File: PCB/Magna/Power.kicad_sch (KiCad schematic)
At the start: 32 parts, among them U902 XL1509-ADJ, U903 WS3222D, U905 AP2171W

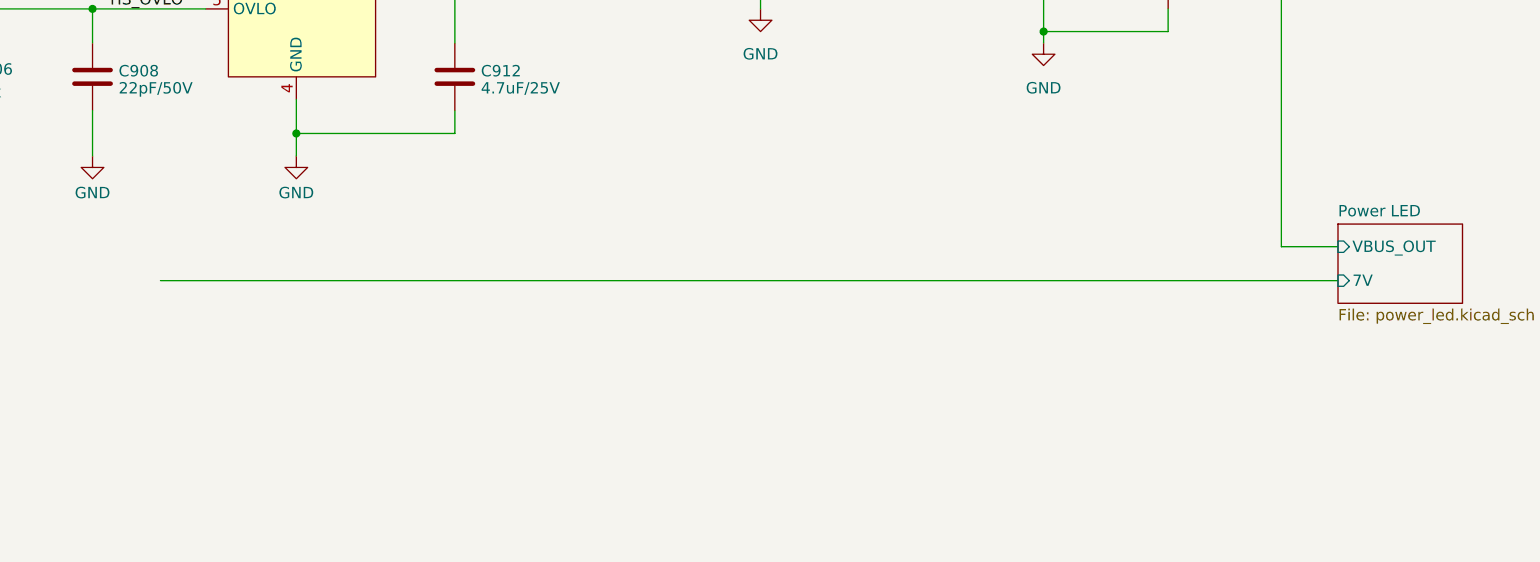
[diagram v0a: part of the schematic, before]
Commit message: Update Audio connector pinning (#14)
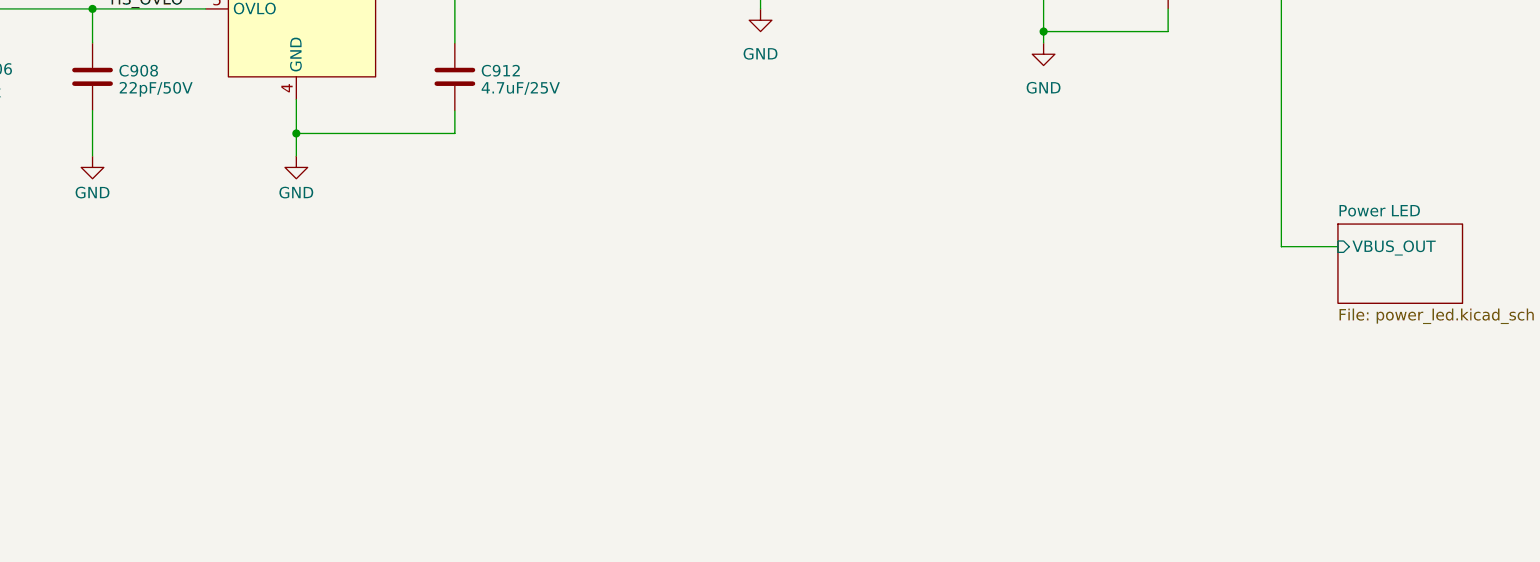
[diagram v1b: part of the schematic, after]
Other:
- sheet Power LED ports: added none; removed 7V
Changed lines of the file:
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@@
-    (stroke (width 0) (type default))
-  )
-  (wire (pts (xy 132.08 80.01) (xy 264.16 80.01))
     (stroke (width 0) (type default))
   )
@@
       (effects (font (size 1.27 1.27)) (justify left top))
     )
-    (pin "7V" input (at 264.16 80.01 180)
-      (effects (font (size 1.27 1.27)) (justify left))
-    )
     (pin "VBUS_OUT" input (at 264.16 76.2 180)

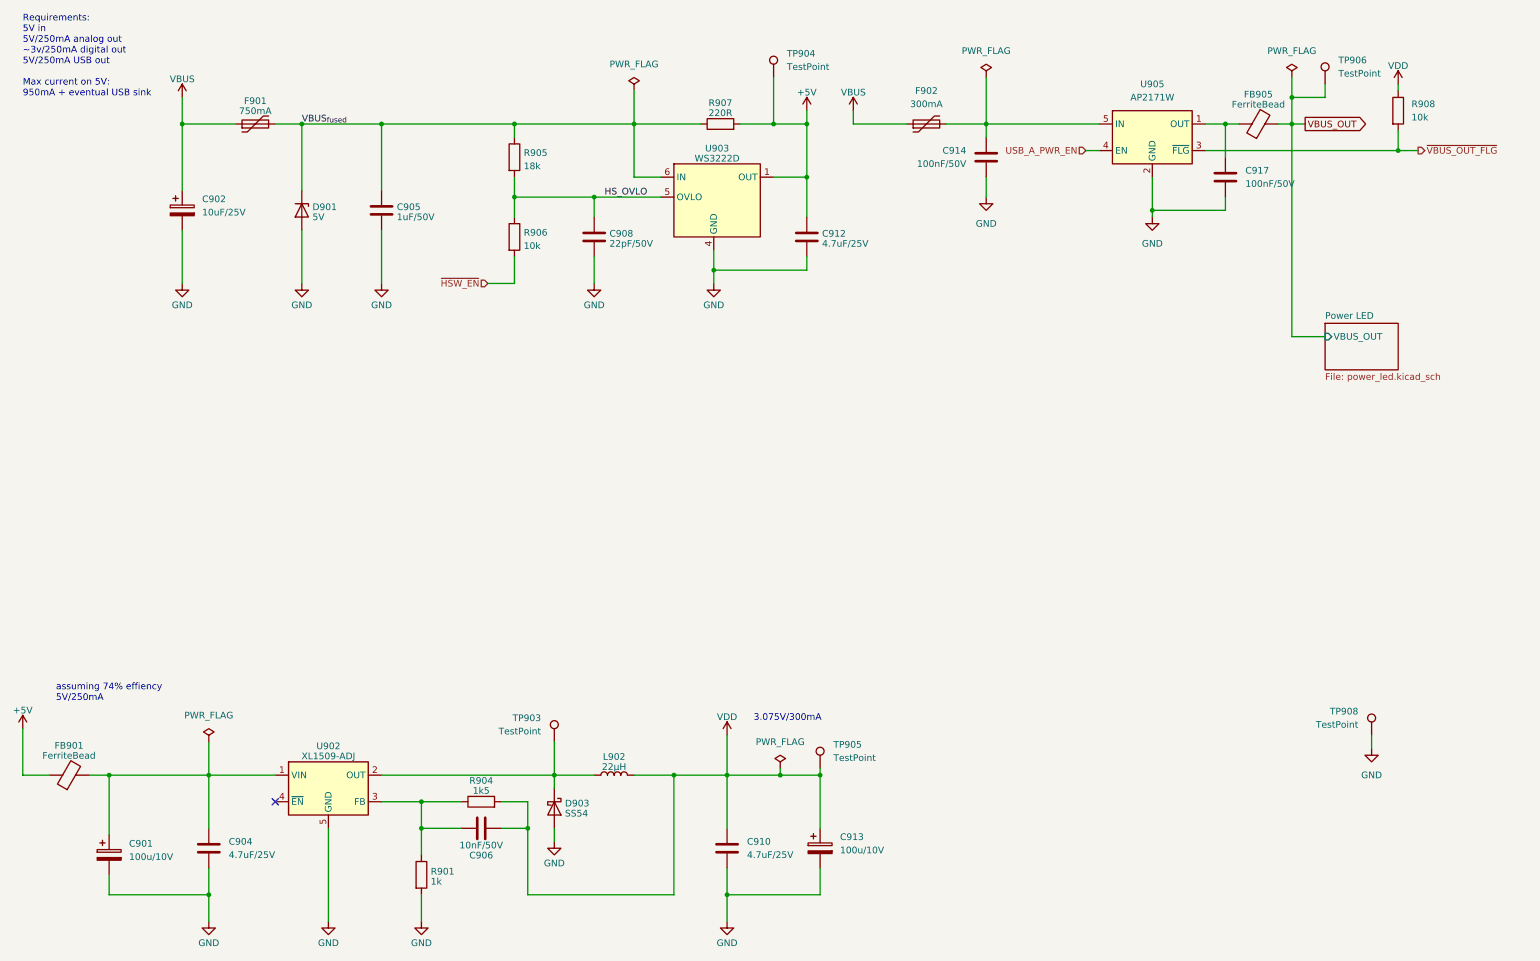
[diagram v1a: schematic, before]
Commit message: Change components on Main Board to use more of the same part#
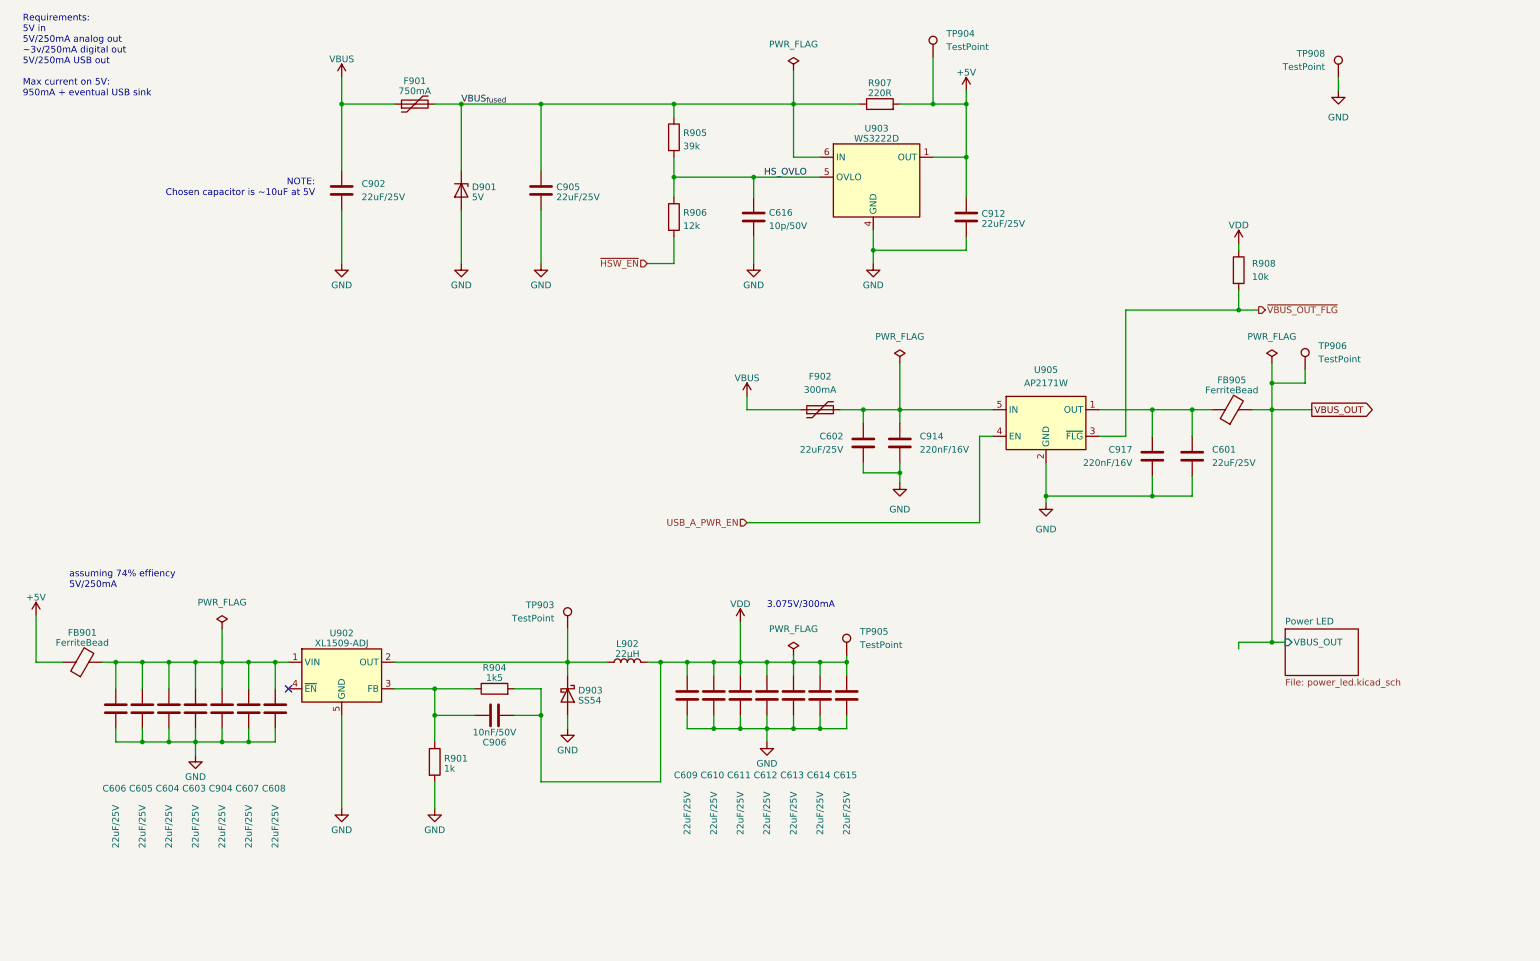
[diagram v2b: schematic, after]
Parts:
- removed C901, C913: 100u/10V, Capacitor_SMD:CP_Elec_6.3x5.8, symbol Device:C_Polarized
- removed C908: 22pF/50V, Capacitor_SMD:C_0805_2012Metric_Pad1.18x1.45mm_HandSolder, symbol Device:C
- removed C910: 4.7uF/25V, Capacitor_SMD:C_0805_2012Metric_Pad1.18x1.45mm_HandSolder, symbol Device:C
- added C601, C602, C603, C604, C605, C606, C607, C608, C609, C610, C611, C612, C613, C614, C615: 22uF/25V, Capacitor_SMD:C_0805_2012Metric_Pad1.18x1.45mm_HandSolder, symbol Device:C
- added C616: 10p/50V, Capacitor_SMD:C_0603_1608Metric_Pad1.08x0.95mm_HandSolder, symbol Device:C
- C902: value 10uF/25V -> 22uF/25V; footprint Capacitor_SMD:CP_Elec_4x5.8 -> Capacitor_SMD:C_0805_2012Metric_Pad1.18x1.45mm_HandSolder; symbol Device:C_Polarized -> Device:C; LCSC C2163094 -> C45783
- C904, C912: value 4.7uF/25V -> 22uF/25V; LCSC C1779 -> C45783
- C905: value 1uF/50V -> 22uF/25V; LCSC C28323 -> C45783
- C914, C917: value 100nF/50V -> 220nF/16V; footprint Capacitor_SMD:C_0805_2012Metric_Pad1.18x1.45mm_HandSolder -> Capacitor_SMD:C_0402_1005Metric_Pad0.74x0.62mm_HandSolder; LCSC C49678 -> C16772
- R905: value 18k -> 39k; footprint Resistor_SMD:R_0603_1608Metric_Pad0.98x0.95mm_HandSolder -> Resistor_SMD:R_0805_2012Metric_Pad1.20x1.40mm_HandSolder; LCSC C25810 -> C17713
- R906: value 10k -> 12k; LCSC C17414 -> C17444
- TP903, TP904, TP905, TP906, TP908: footprint TestPoint:TestPoint_Keystone_5005-5009_Compact -> TestPoint:TestPoint_Keystone_5000-5004_Miniature
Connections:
- net GND: now also C601.2, C602.2, C603.2, C604.2, C605.2, C606.2, C607.2, C608.2, C609.2, C610.2, C611.2, C612.2, C613.2, C614.2, C615.2, C616.1
- net HS_OVLO: now also C616.2
- net VDD: now also C609.1, C610.1, C611.1, C612.1, C613.1, C614.1, C615.1
- net at C904.1, FB901.2, U902.1 (VIN): now also C603.1, C604.1, C605.1, C606.1, C607.1, C608.1
- net at C917.1, FB905.1, U905.1 (OUT): now also C601.1
- net at C914.1, F902.2, U905.5 (IN): now also C602.1
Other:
- note added: "NOTE: Chosen capacitor is ~10uF at 5V"
- moved on the sheet: C904, C905, C906, C912, C914, C917, D901, D903, F901, F902, FB901, FB905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

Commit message: Mainboard layout (#19)
Also adds mounting holes to IO daughterboard
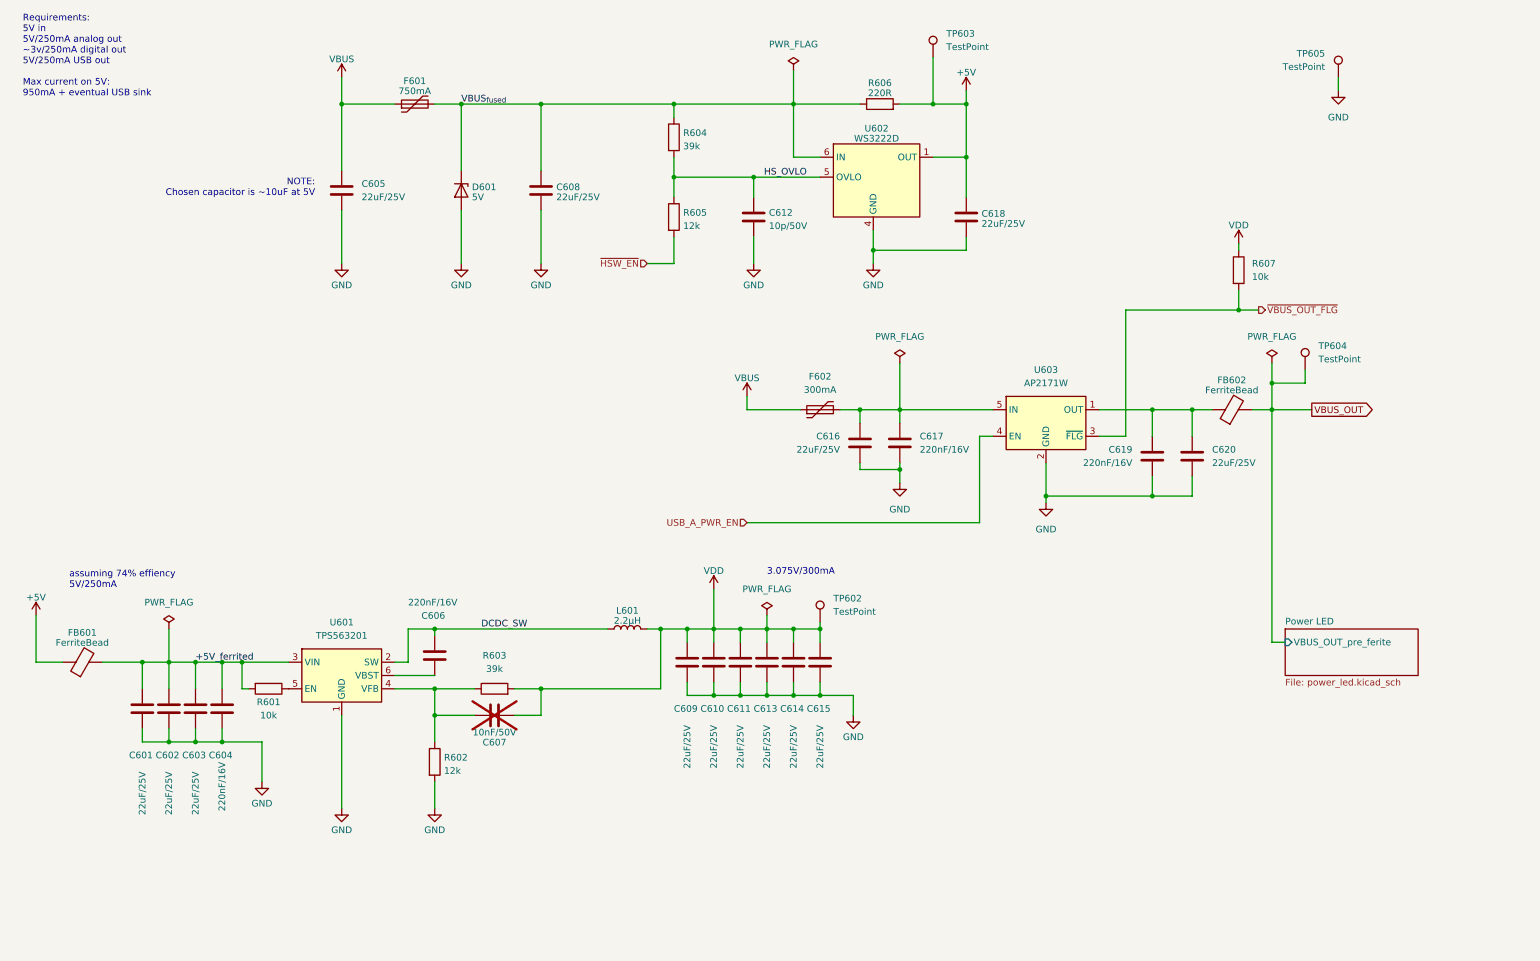
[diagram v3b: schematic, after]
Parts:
- removed C603, C607, C608, C615, C904: 22uF/25V, Capacitor_SMD:C_0805_2012Metric_Pad1.18x1.45mm_HandSolder, symbol Device:C
- removed D903: SS54, Diode_SMD:D_SMA_Handsoldering, symbol Device:D_Schottky
- removed R901: 1k, Resistor_SMD:R_0805_2012Metric_Pad1.20x1.40mm_HandSolder, symbol Device:R
- removed R904: 1k5, Resistor_SMD:R_0805_2012Metric_Pad1.20x1.40mm_HandSolder, symbol Device:R
- removed TP903: TestPoint, TestPoint:TestPoint_Keystone_5000-5004_Miniature, symbol Connector:TestPoint
- removed U902: XL1509-ADJ, Package_SO:SOIC-8_3.9x4.9mm_P1.27mm, symbol Regulator_Switching:XL1509-ADJ
- added C604, C606: 220nF/16V, Capacitor_SMD:C_0402_1005Metric_Pad0.74x0.62mm_HandSolder, symbol Device:C
- added R601: 10k, Resistor_SMD:R_0805_2012Metric_Pad1.20x1.40mm_HandSolder, symbol Device:R
- added R602: 12k, Resistor_SMD:R_0805_2012Metric_Pad1.20x1.40mm_HandSolder, symbol Device:R
- added R603: 39k, Resistor_SMD:R_0805_2012Metric_Pad1.20x1.40mm_HandSolder, symbol Device:R
- added U601: TPS563201, Package_TO_SOT_SMD:SOT-23-6, symbol Regulator_Switching:TPS563200
- C607: renamed from C906; now not fitted
- L601: renamed from L902; value 22µH -> 2.2µH; footprint Skrooter_footprints:MSCD43 -> Inductor_SMD:L_Sunlord_SWPA3012S; LCSC C915172 -> C182126
- renumbered C606 to C601, C605 to C602, C604 to C603, C902 to C605, C905 to C608, C616 to C612, C612 to C613, C613 to C614, C614 to C615, C602 to C616, C914 to C617, C912 to C618, C917 to C619, C601 to C620, D901 to D601, F901 to F601, F902 to F602, FB901 to FB601, FB905 to FB602, R905 to R604, R906 to R605, R907 to R606, R908 to R607, TP905 to TP602, TP904 to TP603, TP906 to TP604, TP908 to TP605, U903 to U602, U905 to U603
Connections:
- net GND: now also C604.2, R602.2, U601.1 (GND)
- net VDD: now also R603.2
- net +5V_ferrited: now reaches C601.1, C602.1, C603.1, FB601.2
- net +5V_ferrited: now also C604.1, R601.2, U601.3 (VIN)
- net DCDC_SW: now reaches L601.1
- net DCDC_SW: now also C606.1, U601.2 (SW)
- net at C607.1: now also R602.1, R603.1, U601.4 (VFB)
- new net: R601.1, U601.5 (EN)
- new net: C606.2, U601.6 (VBST)
- no-connect marks 1 -> 0
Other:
- sheet Power LED ports: added VBUS_OUT_pre_ferite; removed VBUS_OUT
- moved on the sheet: C601, C602, C603, C609, C610, C611, C613, C614, C615, C616, L601, TP602

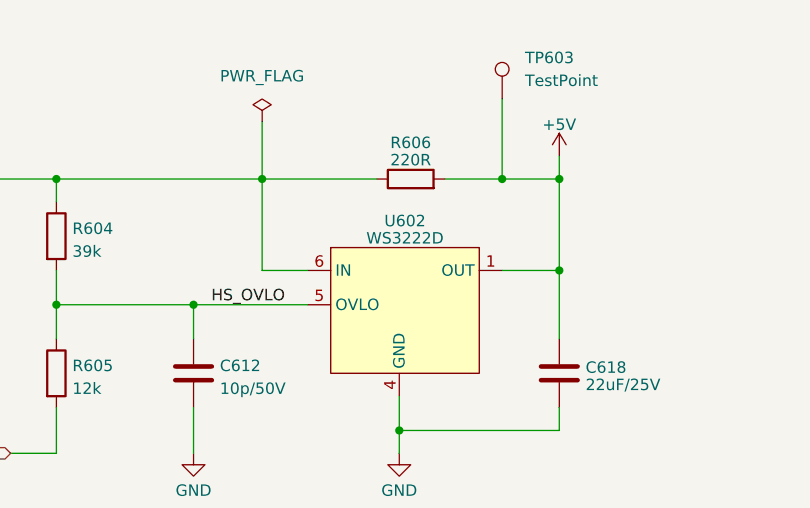
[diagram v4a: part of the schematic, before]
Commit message: Update Project to Kicad 8.0 and prepare for production
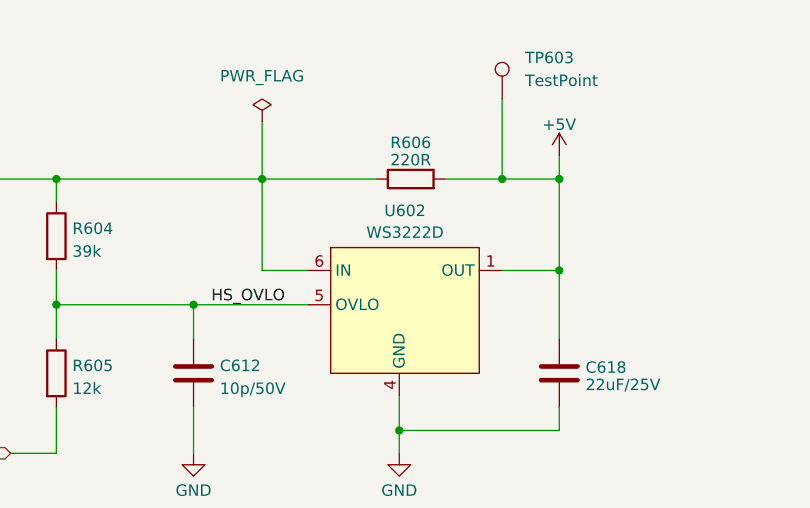
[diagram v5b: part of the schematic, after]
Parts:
- U602: symbol Skrooter_symbols:WS3222D -> SkrooterLib:WS3222D

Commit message: Some updates to PCB
Honestly I cannot remember whats changed
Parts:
- C607: LCSC C3908881 -> C1710
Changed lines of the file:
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@@
 			)
 		)
-		(property "LCSC" "C3908881"
+		(property "LCSC" "C1710"
 			(at 105.41 148.59 90)
 			(effects

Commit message: Update schematics to Kicad 9
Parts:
- U602: symbol SkrooterLib:WS3222D -> Skrooter_symbols:WS3222D
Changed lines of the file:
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@@
 (kicad_sch
-	(version 20231120)
+	(version 20250114)
 	(generator "eeschema")
-	(generator_version "8.0")
+	(generator_version "9.0")
 	(paper "A4")
+	(text "NOTE:\nChosen capacitor is ~10uF at 5V\n"
+		(exclude_from_sim no)
+		(at 71.12 49.53 0)
+		(effects
+			(font
+				(size 1.27 1.27)
+			)
+			(justify right bottom)
+		)
+	)
+	(text "3.075V/300mA"
+		(exclude_from_sim no)
+		(at 157.48 121.92 0)
+		(effects
+			(font
+				(size 1.27 1.27)
+			)
+			(justify left bottom)
+		)
+	)
+	(text "assuming 74% effiency\n5V/250mA"
+		(exclude_from_sim no)
+		(at 24.13 124.46 0)
+		(effects
+			(font
+				(size 1.27 1.27)
+			)
+			(justify left bottom)
+		)
+	)
+	(text "Requirements:\n5V in\n5V/250mA analog out\n~3v/250mA digital out\n5V/250mA USB out\n\nMax current on 5V:\n950mA + eventual USB sink"
+		(exclude_from_sim no)
+		(at 15.24 30.48 0)
+		(effects
+			(font
+				(size 1.27 1.27)
+			)
+			(justify left bottom)
+		)
+	)
 	(junction
 		(at 182.88 101.6)
@@
 		)
 	)
-	(text "NOTE:\nChosen capacitor is ~10uF at 5V\n"
-		(exclude_from_sim no)
-		(at 71.12 49.53 0)
-		(effects
-			(font
-				(size 1.27 1.27)
-			)
-			(justify right bottom)
-		)
-	)
-	(text "3.075V/300mA"
-		(exclude_from_sim no)
-		(at 157.48 121.92 0)
-		(effects
-			(font
-				(size 1.27 1.27)
-			)
-			(justify left bottom)
-		)
-	)
-	(text "assuming 74% effiency\n5V/250mA"
-		(exclude_from_sim no)
-		(at 24.13 124.46 0)
-		(effects
-			(font
-				(size 1.27 1.27)
-			)
-			(justify left bottom)
-		)
-	)
-	(text "Requirements:\n5V in\n5V/250mA analog out\n~3v/250mA digital out\n5V/250mA USB out\n\nMax current on 5V:\n950mA + eventual USB sink"
-		(exclude_from_sim no)
-		(at 15.24 30.48 0)
-		(effects
-			(font
-				(size 1.27 1.27)
-			)
-			(justify left bottom)
-		)
-	)
 	(label "DCDC_SW"
 		(at 102.87 132.08 0)
-		(fields_autoplaced yes)
 		(effects
 			(font
@@
 	(label "+5V_ferrited"
 		(at 48.26 138.43 0)
-		(fields_autoplaced yes)
 		(effects
 			(font
@@
 	(label "VBUS_{fused}"
 		(at 99.06 31.75 0)
-		(fields_autoplaced yes)
 		(effects
 			(font
@@
 	(label "HS_OVLO"
 		(at 165.1 45.72 180)
-		(fields_autoplaced yes)
 		(effects
 			(font
@@
 		(shape input)
 		(at 153.67 111.76 180)
-		(fields_autoplaced yes)
 		(effects
 			(font
@@
 		(shape input)
 		(at 134.62 62.23 180)
-		(fields_autoplaced yes)
 		(effects
 			(font
@@
 		(shape output)
 		(at 251.46 71.12 0)
-		(fields_autoplaced yes)
 		(effects
 			(font
@@
 	)
 	(symbol
-		(lib_id "SkrooterLib:WS3222D")
+		(lib_id "Skrooter_symbols:WS3222D")
 		(at 177.8 39.37 0)
 		(unit 1)
@@
 		(at 256.54 132.08)
 		(size 25.4 8.89)
+		(exclude_from_sim no)
+		(in_bom yes)
+		(on_board yes)
+		(dnp no)
 		(fields_autoplaced yes)
 		(stroke
